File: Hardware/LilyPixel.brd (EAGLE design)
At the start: 20 x 20 mm, 12 parts

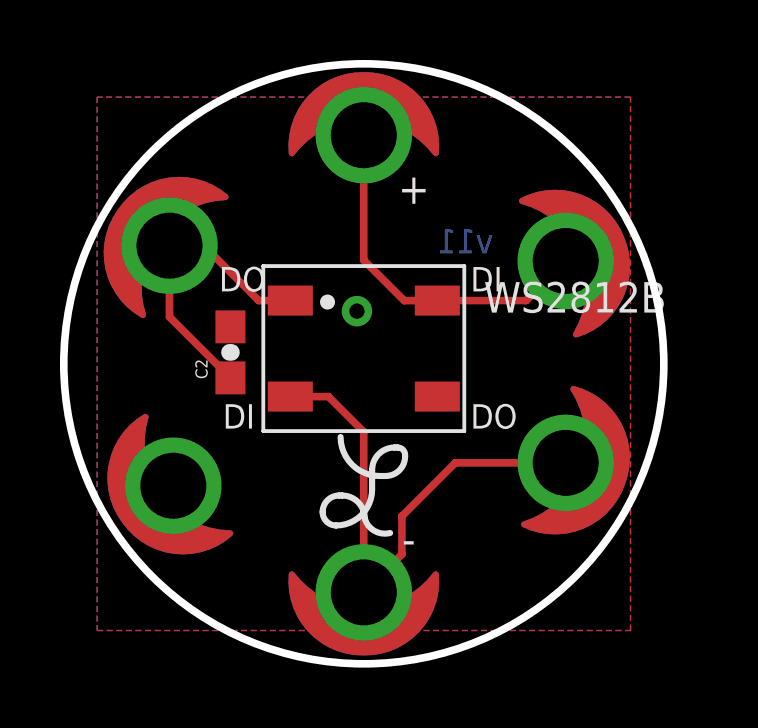
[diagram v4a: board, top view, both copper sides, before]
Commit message: LED/Silk Orientation
Fixed the orientation of the silk, LED and petals.

Added Sparkfun Flame
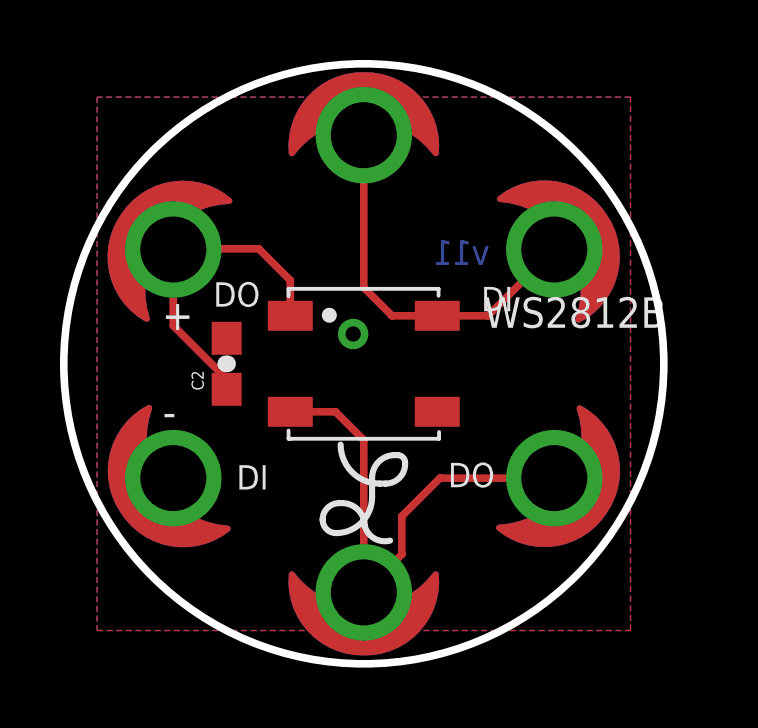
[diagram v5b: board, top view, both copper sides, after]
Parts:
- added U$2: (no value), SparkFun-Aesthetics:SFE_LOGO_FLAME_.1
- moved U$12 0.64 mm to (6.35, -3.81), turned to 56 degrees
- moved U$10 0.54 mm to (6.35, 3.81), turned to 123 degrees
- moved WS2812B 0.51 mm to (0.00, 0.00)
- moved C2 0.40 mm to (-4.57, 0.00)
- moved U$14 0.25 mm to (-6.35, -3.81), turned to 303 degrees
- moved U$8 0.25 mm to (0.00, -4.32)
- moved U$13 0.18 mm to (-6.35, 3.81)
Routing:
- net DO1: track 17.6 -> 16.6 mm
- net VCC: track 10.0 -> 10.9 mm
- net DI1: track 12.0 -> 12.7 mm
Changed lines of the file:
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@@
 <setting verticaltext="up"/>
 </settings>
-<grid distance="0.05" unitdist="inch" unit="inch" style="lines" multiple="1" display="yes" altdistance="0.005" altunitdist="inch" altunit="inch"/>
+<grid distance="0.05" unitdist="inch" unit="inch" style="lines" multiple="1" display="yes" altdistance="0.001" altunitdist="inch" altunit="inch"/>
 <layers>
 <layer number="1" name="Top" color="4" fill="1" visible="yes" active="yes"/>
@@
 <circle x="0" y="0" radius="4.5" width="0.0508" layer="47"/>
 <circle x="0" y="0" radius="10" width="0.254" layer="20"/>
-<text x="1.143" y="5.334" size="1.016" layer="21" font="vector" ratio="15">+</text>
-<text x="1.27" y="-6.35" size="1.016" layer="21" font="vector" ratio="15">-</text>
+<text x="-6.731" y="1.1176" size="1.016" layer="21" font="vector" ratio="15">+</text>
+<text x="-6.7056" y="-2.1082" size="1.016" layer="21" font="vector" ratio="15">-</text>
 <text x="33.02" y="-33.02" size="1.778" layer="27" font="vector" ratio="15">M. HORD</text>
 <polygon width="0.2032" layer="29">
@@
 <vertex x="0" y="-8.2"/>
 </polygon>
-<text x="-4.826" y="2.413" size="0.8128" layer="21" font="vector" ratio="15">DO</text>
-<text x="3.556" y="-2.159" size="0.8128" layer="21" font="vector" ratio="15">DO</text>
-<text x="3.556" y="2.413" size="0.8128" layer="21" font="vector" ratio="15">DI</text>
-<text x="-4.699" y="-2.159" size="0.8128" layer="21" font="vector" ratio="15">DI</text>
-<text x="4.318" y="3.683" size="0.8128" layer="16" font="vector" ratio="15" rot="MR0">v11</text>
+<text x="-3.4544" y="2.7178" size="0.8128" layer="21" font="vector" ratio="15" rot="R180">DO</text>
+<text x="4.3688" y="-3.302" size="0.8128" layer="21" font="vector" ratio="15" rot="R180">DO</text>
+<text x="3.9116" y="1.7526" size="0.8128" layer="21" font="vector" ratio="15">DI</text>
+<text x="-3.175" y="-3.3782" size="0.8128" layer="21" font="vector" ratio="15" rot="R180">DI</text>
+<text x="4.191" y="3.302" size="0.8128" layer="16" font="vector" ratio="15" rot="MR0">v11</text>
 <text x="3.81" y="-25.4" size="1.778" layer="51" font="vector" ratio="10">Mike Hord</text>
 <text x="-15.24" y="-27.94" size="1.778" layer="51" font="vector" ratio="10">Revised by: Patrick Alberts</text>
@@
 </autorouter>
 <elements>
-<element name="U$8" library="LilyPad-Wearables" package="LOGO-L" value="LOGO-LPL" x="0" y="-4.064"/>
+<element name="U$8" library="LilyPad-Wearables" package="LOGO-L" value="LOGO-LPL" x="0" y="-4.318"/>
 <element name="FRAME1" library="SparkFun-Aesthetics" package="CREATIVE_COMMONS" value="FRAME-LETTER" x="-26.67" y="-25.4"/>
 <element name="U$1" library="LilyPad-Wearables" package="LOGO-LILYPAD" value="LOGO-LPLP" x="0" y="0" rot="MR0"/>
-<element name="WS2812B" library="SparkFun-LED" package="WS2812B" value="" x="0" y="0.508"/>
+<element name="WS2812B" library="SparkFun-LED" package="WS2812B" value="" x="0" y="0"/>
 <element name="U$9" library="LilyPad-Wearables" package="PETAL-SMALL-2SIDE" value="SEWTAP6" x="0" y="7.62" rot="R180"/>
-<element name="U$10" library="LilyPad-Wearables" package="PETAL-SMALL-2SIDE" value="SEWTAP6" x="6.731" y="3.429" rot="SR112"/>
+<element name="U$10" library="LilyPad-Wearables" package="PETAL-SMALL-2SIDE" value="SEWTAP6" x="6.35" y="3.81" rot="SR123"/>
 <element name="U$11" library="LilyPad-Wearables" package="PETAL-SMALL-2SIDE" value="SEWTAP6" x="0" y="-7.62"/>
-<element name="U$12" library="LilyPad-Wearables" package="PETAL-SMALL-2SIDE" value="SEWTAP6" x="6.731" y="-3.302" rot="R70"/>
-<element name="U$13" library="LilyPad-Wearables" package="PETAL-SMALL-2SIDE" value="SEWTAP6" x="-6.477" y="3.937" rot="R235"/>
-<element name="C2" library="SparkFun-Capacitors" package="0603-CAP" value="0.1uF" x="-4.445" y="0.381" rot="R90">
-<attribute name="PROD_ID" value="CAP-00810" x="-4.445" y="0.381" size="1.778" layer="27" font="vector" ratio="15" rot="R90" display="off"/>
+<element name="U$12" library="LilyPad-Wearables" package="PETAL-SMALL-2SIDE" value="SEWTAP6" x="6.35" y="-3.81" rot="R56"/>
+<element name="U$13" library="LilyPad-Wearables" package="PETAL-SMALL-2SIDE" value="SEWTAP6" x="-6.35" y="3.81" rot="R235"/>
+<element name="C2" library="SparkFun-Capacitors" package="0603-CAP" value="0.1uF" x="-4.572" y="0" rot="R90">
+<attribute name="PROD_ID" value="CAP-00810" x="-4.572" y="0" size="1.778" layer="27" font="vector" ratio="15" rot="R90" display="off"/>
 </element>
-<element name="U$14" library="LilyPad-Wearables" package="PETAL-SMALL-2SIDE" value="SEWTAP6" x="-6.35" y="-4.064" rot="R306"/>
+<element name="U$14" library="LilyPad-Wearables" package="PETAL-SMALL-2SIDE" value="SEWTAP6" x="-6.35" y="-3.81" rot="R303"/>
 <element name="LOGO1" library="SparkFun-Aesthetics" package="OSHW-LOGO-S" value="OSHW-LOGOS" x="0" y="3.81" rot="MR0"/>
+<element name="U$2" library="SparkFun-Aesthetics" package="SFE_LOGO_FLAME_.1" value="" x="1.016" y="-6.096" rot="MR0"/>
 </elements>
 <signals>
@@
 <contactref element="C2" pad="1"/>
 <contactref element="WS2812B" pad="1"/>
-<wire x1="-2.4502" y1="2.1082" x2="-2.45" y2="2.108" width="0.254" layer="1"/>
-<wire x1="-2.4502" y1="2.1082" x2="-3.5052" y2="2.1082" width="0.254" layer="1"/>
-<wire x1="-3.5052" y1="2.1082" x2="-5.334" y2="3.937" width="0.254" layer="1"/>
-<wire x1="-5.334" y1="3.937" x2="-6.477" y2="3.937" width="0.254" layer="1"/>
-<wire x1="-6.477" y1="3.937" x2="-6.477" y2="1.563" width="0.254" layer="1"/>
-<wire x1="-6.477" y1="1.563" x2="-4.445" y2="-0.469" width="0.254" layer="1"/>
+<wire x1="-4.572" y1="-0.85" x2="-4.572" y2="-0.508" width="0.254" layer="1"/>
+<wire x1="-4.572" y1="-0.508" x2="-6.35" y2="1.27" width="0.254" layer="1"/>
+<wire x1="-6.35" y1="1.27" x2="-6.35" y2="3.81" width="0.254" layer="1"/>
+<wire x1="-2.45" y1="1.6" x2="-2.45" y2="2.7802" width="0.254" layer="1"/>
+<wire x1="-2.45" y1="2.7802" x2="-3.5052" y2="3.8354" width="0.254" layer="1"/>
+<wire x1="-3.5052" y1="3.8354" x2="-6.3246" y2="3.8354" width="0.254" layer="1"/>
+<wire x1="-6.3246" y1="3.8354" x2="-6.35" y2="3.81" width="0.254" layer="1"/>
 </signal>
 <signal name="GND">
@@
 <vertex x="8.89" y="8.89"/>
 </polygon>
-<via x="-0.2286" y="1.755140625" extent="1-16" drill="0.508"/>
+<via x="-0.3556" y="0.993140625" extent="1-16" drill="0.508"/>
 <contactref element="C2" pad="2"/>
 <contactref element="WS2812B" pad="3"/>
@@
 <contactref element="U$10" pad="1"/>
 <contactref element="WS2812B" pad="4"/>
-<wire x1="2.45" y1="2.108" x2="5.41" y2="2.108" width="0.254" layer="1"/>
-<wire x1="5.41" y1="2.108" x2="6.731" y2="3.429" width="0.254" layer="1"/>
-<wire x1="0" y1="7.62" x2="0" y2="3.4544" width="0.254" layer="1"/>
-<wire x1="0" y1="3.4544" x2="1.348740625" y2="2.105659375" width="0.254" layer="1"/>
-<wire x1="1.348740625" y1="2.105659375" x2="2.447659375" y2="2.105659375" width="0.254" layer="1"/>
-<wire x1="2.447659375" y1="2.105659375" x2="2.45" y2="2.108" width="0.254" layer="1"/>
+<wire x1="2.45" y1="1.6" x2="0.94" y2="1.6" width="0.254" layer="1"/>
+<wire x1="0.94" y1="1.6" x2="0" y2="2.54" width="0.254" layer="1"/>
+<wire x1="0" y1="2.54" x2="0" y2="7.62" width="0.254" layer="1"/>
+<wire x1="2.45" y1="1.6" x2="4.14" y2="1.6" width="0.254" layer="1"/>
+<wire x1="4.14" y1="1.6" x2="6.35" y2="3.81" width="0.254" layer="1"/>
 </signal>
 <signal name="DO1">
@@
 <contactref element="U$11" pad="1"/>
 <contactref element="WS2812B" pad="2"/>
-<wire x1="0" y1="-7.62" x2="0" y2="-2.270759375" width="0.254" layer="1"/>
-<wire x1="0" y1="-2.270759375" x2="-1.178559375" y2="-1.0922" width="0.254" layer="1"/>
-<wire x1="-1.178559375" y1="-1.0922" x2="-2.4498" y2="-1.0922" width="0.254" layer="1"/>
-<wire x1="-2.4498" y1="-1.0922" x2="-2.45" y2="-1.092" width="0.254" layer="1"/>
+<wire x1="-2.45" y1="-1.6" x2="-0.94" y2="-1.6" width="0.254" layer="1"/>
+<wire x1="-0.94" y1="-1.6" x2="0" y2="-2.54" width="0.254" layer="1"/>
+<wire x1="0" y1="-2.54" x2="0" y2="-7.62" width="0.254" layer="1"/>
 <wire x1="0" y1="-7.62" x2="1.27" y2="-6.35" width="0.254" layer="1"/>
 <wire x1="1.27" y1="-6.35" x2="1.27" y2="-5.08" width="0.254" layer="1"/>
-<wire x1="1.27" y1="-5.08" x2="3.048" y2="-3.302" width="0.254" layer="1"/>
-<wire x1="3.048" y1="-3.302" x2="6.731" y2="-3.302" width="0.254" layer="1"/>
+<wire x1="1.27" y1="-5.08" x2="2.54" y2="-3.81" width="0.254" layer="1"/>
+<wire x1="2.54" y1="-3.81" x2="6.35" y2="-3.81" width="0.254" layer="1"/>
 </signal>
 </signals>

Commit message: Re assigned Petals, full complete re route.
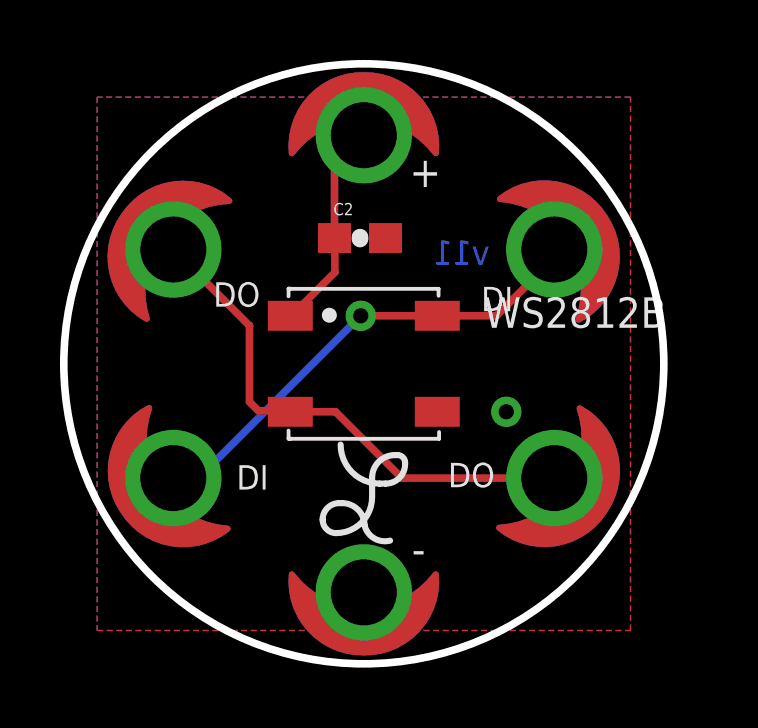
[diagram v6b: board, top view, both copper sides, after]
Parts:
- moved C2 6.11 mm to (-0.13, 4.19), turned to 0 degrees
- renumbered U$10 to JP5, U$11 to JP3, U$12 to JP2, U$13 to JP1, U$14 to JP6, U$9 to JP4
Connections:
- net DI1: now also JP6.1; no longer JP4.1
- net DO1: now also JP1.1; no longer JP3.1
- net GND: now also JP3.1; no longer JP6.1
- net VCC: now also JP4.1; no longer JP1.1
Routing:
- net VCC: track 10.9 -> 7.07 mm
- net DI1: track 12.7 -> 16.0 mm, vias 0 -> 1
- net DO1: track 16.6 -> 17.4 mm
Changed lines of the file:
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@@
 <circle x="0" y="0" radius="4.5" width="0.0508" layer="47"/>
 <circle x="0" y="0" radius="10" width="0.254" layer="20"/>
-<text x="-6.731" y="1.1176" size="1.016" layer="21" font="vector" ratio="15">+</text>
-<text x="-6.7056" y="-2.1082" size="1.016" layer="21" font="vector" ratio="15">-</text>
+<text x="1.524" y="5.8928" size="1.016" layer="21" font="vector" ratio="15">+</text>
+<text x="1.6002" y="-6.6802" size="1.016" layer="21" font="vector" ratio="15">-</text>
 <text x="33.02" y="-33.02" size="1.778" layer="27" font="vector" ratio="15">M. HORD</text>
 <polygon width="0.2032" layer="29">
@@
 <element name="U$1" library="LilyPad-Wearables" package="LOGO-LILYPAD" value="LOGO-LPLP" x="0" y="0" rot="MR0"/>
 <element name="WS2812B" library="SparkFun-LED" package="WS2812B" value="" x="0" y="0"/>
-<element name="U$9" library="LilyPad-Wearables" package="PETAL-SMALL-2SIDE" value="SEWTAP6" x="0" y="7.62" rot="R180"/>
-<element name="U$10" library="LilyPad-Wearables" package="PETAL-SMALL-2SIDE" value="SEWTAP6" x="6.35" y="3.81" rot="SR123"/>
-<element name="U$11" library="LilyPad-Wearables" package="PETAL-SMALL-2SIDE" value="SEWTAP6" x="0" y="-7.62"/>
-<element name="U$12" library="LilyPad-Wearables" package="PETAL-SMALL-2SIDE" value="SEWTAP6" x="6.35" y="-3.81" rot="R56"/>
-<element name="U$13" library="LilyPad-Wearables" package="PETAL-SMALL-2SIDE" value="SEWTAP6" x="-6.35" y="3.81" rot="R235"/>
-<element name="C2" library="SparkFun-Capacitors" package="0603-CAP" value="0.1uF" x="-4.572" y="0" rot="R90">
-<attribute name="PROD_ID" value="CAP-00810" x="-4.572" y="0" size="1.778" layer="27" font="vector" ratio="15" rot="R90" display="off"/>
+<element name="JP4" library="LilyPad-Wearables" package="PETAL-SMALL-2SIDE" value="SEWTAP6" x="0" y="7.62" rot="R180"/>
+<element name="JP5" library="LilyPad-Wearables" package="PETAL-SMALL-2SIDE" value="SEWTAP6" x="6.35" y="3.81" rot="SR123"/>
+<element name="JP3" library="LilyPad-Wearables" package="PETAL-SMALL-2SIDE" value="SEWTAP6" x="0" y="-7.62"/>
+<element name="JP2" library="LilyPad-Wearables" package="PETAL-SMALL-2SIDE" value="SEWTAP6" x="6.35" y="-3.81" rot="R56"/>
+<element name="JP1" library="LilyPad-Wearables" package="PETAL-SMALL-2SIDE" value="SEWTAP6" x="-6.35" y="3.81" rot="R235"/>
+<element name="C2" library="SparkFun-Capacitors" package="0603-CAP" value="0.1uF" x="-0.127" y="4.191">
+<attribute name="PROD_ID" value="CAP-00810" x="-0.127" y="4.191" size="1.778" layer="27" font="vector" ratio="15" display="off"/>
 </element>
-<element name="U$14" library="LilyPad-Wearables" package="PETAL-SMALL-2SIDE" value="SEWTAP6" x="-6.35" y="-3.81" rot="R303"/>
+<element name="JP6" library="LilyPad-Wearables" package="PETAL-SMALL-2SIDE" value="SEWTAP6" x="-6.35" y="-3.81" rot="R303"/>
 <element name="LOGO1" library="SparkFun-Aesthetics" package="OSHW-LOGO-S" value="OSHW-LOGOS" x="0" y="3.81" rot="MR0"/>
 <element name="U$2" library="SparkFun-Aesthetics" package="SFE_LOGO_FLAME_.1" value="" x="1.016" y="-6.096" rot="MR0"/>
@@
 <signals>
 <signal name="VCC">
-<contactref element="U$13" pad="1"/>
 <contactref element="C2" pad="1"/>
 <contactref element="WS2812B" pad="1"/>
-<wire x1="-4.572" y1="-0.85" x2="-4.572" y2="-0.508" width="0.254" layer="1"/>
-<wire x1="-4.572" y1="-0.508" x2="-6.35" y2="1.27" width="0.254" layer="1"/>
-<wire x1="-6.35" y1="1.27" x2="-6.35" y2="3.81" width="0.254" layer="1"/>
-<wire x1="-2.45" y1="1.6" x2="-2.45" y2="2.7802" width="0.254" layer="1"/>
-<wire x1="-2.45" y1="2.7802" x2="-3.5052" y2="3.8354" width="0.254" layer="1"/>
-<wire x1="-3.5052" y1="3.8354" x2="-6.3246" y2="3.8354" width="0.254" layer="1"/>
-<wire x1="-6.3246" y1="3.8354" x2="-6.35" y2="3.81" width="0.254" layer="1"/>
+<contactref element="JP4" pad="1"/>
+<wire x1="-0.977" y1="4.191" x2="-0.977" y2="6.643" width="0.254" layer="1"/>
+<wire x1="-0.977" y1="6.643" x2="0" y2="7.62" width="0.254" layer="1"/>
+<wire x1="-2.45" y1="1.6" x2="-2.4132" y2="1.6" width="0.254" layer="1"/>
+<wire x1="-2.4132" y1="1.6" x2="-0.9652" y2="3.048" width="0.254" layer="1"/>
+<wire x1="-0.9652" y1="3.048" x2="-0.9652" y2="4.1792" width="0.254" layer="1"/>
+<wire x1="-0.9652" y1="4.1792" x2="-0.977" y2="4.191" width="0.254" layer="1"/>
 </signal>
 <signal name="GND">
@@
 <vertex x="8.89" y="8.89"/>
 </polygon>
-<via x="-0.3556" y="0.993140625" extent="1-16" drill="0.508"/>
 <contactref element="C2" pad="2"/>
 <contactref element="WS2812B" pad="3"/>
-<contactref element="U$14" pad="1"/>
+<contactref element="JP3" pad="1"/>
+<via x="4.7498" y="-1.6002" extent="1-16" drill="0.508"/>
 </signal>
 <signal name="N$7">
@@
 </signal>
 <signal name="DI1">
-<contactref element="U$9" pad="1"/>
-<contactref element="U$10" pad="1"/>
+<contactref element="JP5" pad="1"/>
 <contactref element="WS2812B" pad="4"/>
-<wire x1="2.45" y1="1.6" x2="0.94" y2="1.6" width="0.254" layer="1"/>
-<wire x1="0.94" y1="1.6" x2="0" y2="2.54" width="0.254" layer="1"/>
-<wire x1="0" y1="2.54" x2="0" y2="7.62" width="0.254" layer="1"/>
-<wire x1="2.45" y1="1.6" x2="4.14" y2="1.6" width="0.254" layer="1"/>
-<wire x1="4.14" y1="1.6" x2="6.35" y2="3.81" width="0.254" layer="1"/>
+<contactref element="JP6" pad="1"/>
+<wire x1="6.35" y1="3.81" x2="6.35" y2="3.5306" width="0.254" layer="1"/>
+<wire x1="6.35" y1="3.5306" x2="4.4196" y2="1.6002" width="0.254" layer="1"/>
+<wire x1="4.4196" y1="1.6002" x2="2.4502" y2="1.6002" width="0.254" layer="1"/>
+<wire x1="2.4502" y1="1.6002" x2="2.45" y2="1.6" width="0.254" layer="1"/>
+<via x="-0.1016" y="1.6002" extent="1-16" drill="0.508"/>
+<wire x1="-0.1016" y1="1.6002" x2="2.4498" y2="1.6002" width="0.254" layer="1"/>
+<wire x1="2.4498" y1="1.6002" x2="2.45" y2="1.6" width="0.254" layer="1"/>
+<wire x1="-6.35" y1="-3.81" x2="-5.5118" y2="-3.81" width="0.254" layer="16"/>
+<wire x1="-5.5118" y1="-3.81" x2="-0.1016" y2="1.6002" width="0.254" layer="16"/>
 </signal>
 <signal name="DO1">
-<contactref element="U$12" pad="1"/>
-<contactref element="U$11" pad="1"/>
+<contactref element="JP2" pad="1"/>
 <contactref element="WS2812B" pad="2"/>
+<contactref element="JP1" pad="1"/>
 <wire x1="-2.45" y1="-1.6" x2="-0.94" y2="-1.6" width="0.254" layer="1"/>
-<wire x1="-0.94" y1="-1.6" x2="0" y2="-2.54" width="0.254" layer="1"/>
-<wire x1="0" y1="-2.54" x2="0" y2="-7.62" width="0.254" layer="1"/>
-<wire x1="0" y1="-7.62" x2="1.27" y2="-6.35" width="0.254" layer="1"/>
-<wire x1="1.27" y1="-6.35" x2="1.27" y2="-5.08" width="0.254" layer="1"/>
-<wire x1="1.27" y1="-5.08" x2="2.54" y2="-3.81" width="0.254" layer="1"/>
-<wire x1="2.54" y1="-3.81" x2="6.35" y2="-3.81" width="0.254" layer="1"/>
+<wire x1="-0.94" y1="-1.6" x2="1.27" y2="-3.81" width="0.254" layer="1"/>
+<wire x1="1.27" y1="-3.81" x2="6.35" y2="-3.81" width="0.254" layer="1"/>
+<wire x1="-2.413" y1="-1.563" x2="-2.45" y2="-1.6" width="0.254" layer="1"/>
+<wire x1="-2.413" y1="-1.563" x2="-3.517" y2="-1.563" width="0.254" layer="1"/>
+<wire x1="-3.517" y1="-1.563" x2="-3.81" y2="-1.27" width="0.254" layer="1"/>
+<wire x1="-3.81" y1="-1.27" x2="-3.81" y2="1.27" width="0.254" layer="1"/>
+<wire x1="-3.81" y1="1.27" x2="-6.35" y2="3.81" width="0.254" layer="1"/>
 </signal>
 </signals>
